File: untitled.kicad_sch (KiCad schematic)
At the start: 39 parts, among them U17 OPA388, U3 MAX9939, U4 TLV3501AID, U5 DGS0010A, U7 ADC10065

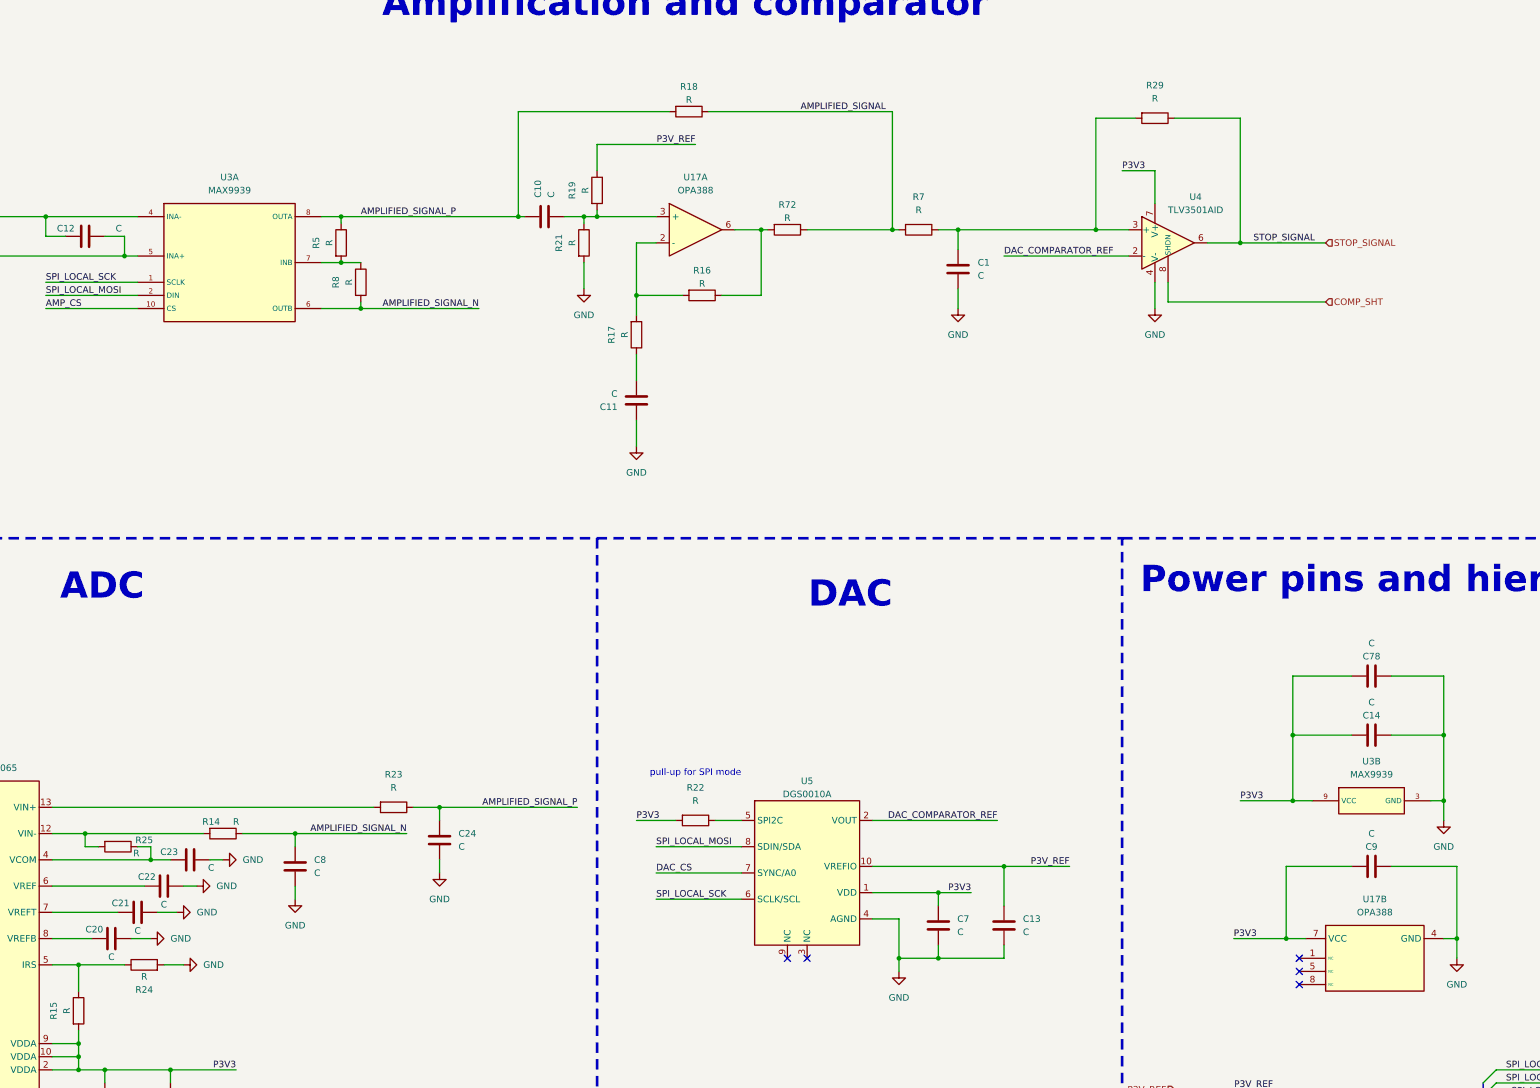
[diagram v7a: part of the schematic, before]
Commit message: most values in schematic filled corrected footprint mistake
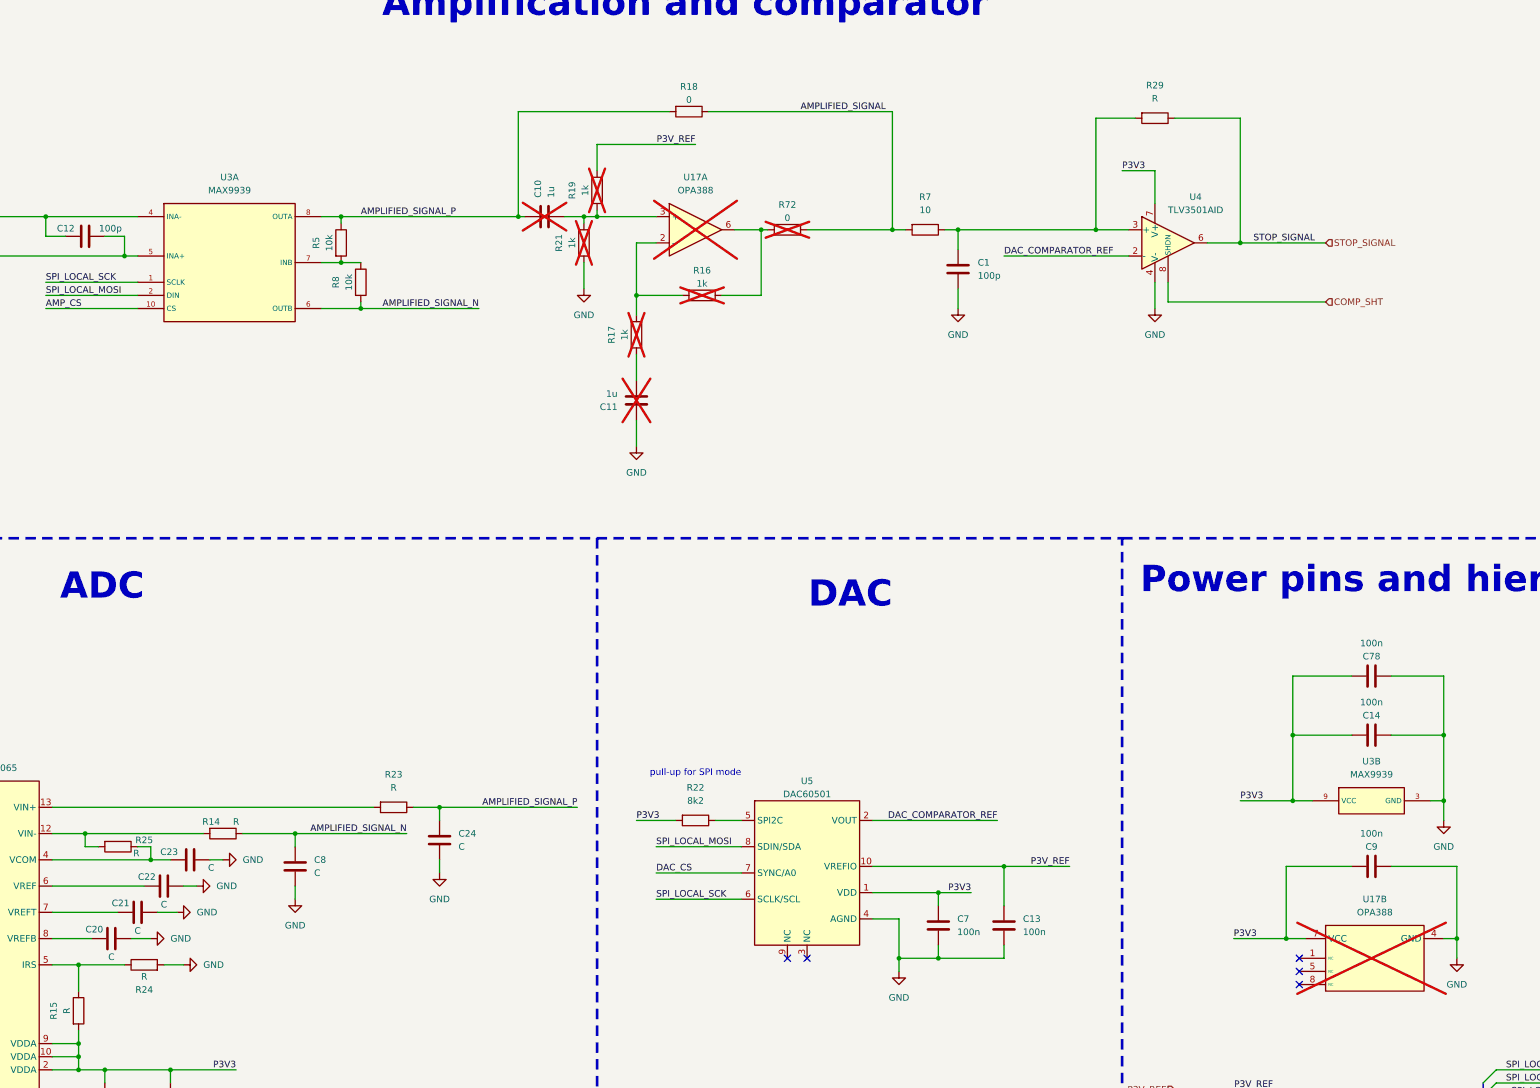
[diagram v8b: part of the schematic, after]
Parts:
- C1, C12: value C -> 100p
- C10, C11: value C -> 1u; now not fitted
- C13, C14, C7, C78, C9: value C -> 100n
- R16, R17, R19, R21: value R -> 1k; now not fitted
- R18: value R -> 0
- R22: value R -> 8k2
- R5, R8: value R -> 10k
- R7: value R -> 10
- R72: value R -> 0; now not fitted
- U17: now not fitted
- U5: value DGS0010A -> DAC60501
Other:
- moved on the sheet: R7
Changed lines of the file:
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@@
 	(wire
 		(pts
-			(xy 255.27 67.31) (xy 256.54 67.31)
+			(xy 255.27 67.31) (xy 257.81 67.31)
 		)
 		(stroke
@@
 	(wire
 		(pts
-			(xy 264.16 67.31) (xy 267.97 67.31)
+			(xy 265.43 67.31) (xy 267.97 67.31)
 		)
 		(stroke
@@
 		(in_bom yes)
 		(on_board yes)
-		(dnp no)
+		(dnp yes)
 		(property "Reference" "R21"
 			(at 190.754 69.85 90)
@@
 			)
 		)
-		(property "Value" "R"
+		(property "Value" "1k"
 			(at 193.294 69.85 90)
 			(effects
@@
 			)
 		)
-		(property "Value" "R"
+		(property "Value" "10k"
 			(at 146.304 69.85 90)
 			(effects
@@
 		(in_bom yes)
 		(on_board yes)
-		(dnp no)
+		(dnp yes)
 		(fields_autoplaced yes)
 		(property "Reference" "U17"
@@
 			)
 		)
-		(property "Datasheet" ""
+		(property "Datasheet" "https://cz.mouser.com/ProductDetail/Texas-Instruments/OPA388IDGKR?qs=sGAEpiMZZMutXGli8Ay4kEuv900fs2zN%2FP2E49NQzzw%3D"
 			(at 212.09 62.23 0)
 			(effects
@@
 		(in_bom yes)
 		(on_board yes)
-		(dnp no)
+		(dnp yes)
 		(fields_autoplaced yes)
 		(property "Reference" "U17"
@@
 			)
 		)
-		(property "Datasheet" ""
+		(property "Datasheet" "https://cz.mouser.com/ProductDetail/Texas-Instruments/OPA388IDGKR?qs=sGAEpiMZZMutXGli8Ay4kEuv900fs2zN%2FP2E49NQzzw%3D"
 			(at 339.09 201.93 0)
 			(effects
@@
 			)
 		)
-		(property "Datasheet" ""
+		(property "Datasheet" "https://cz.mouser.com/ProductDetail/Analog-Devices-Maxim-Integrated/MAX9939AUB%2bT?qs=1eQvB6Dk1vhzbg6od%2Fp2zg%3D%3D"
 			(at 114.3 62.23 0)
 			(effects
@@
 			)
 		)
-		(property "Value" "C"
+		(property "Value" "100n"
 			(at 347.98 184.15 90)
 			(effects
@@
 			)
 		)
-		(property "Value" "C"
+		(property "Value" "100n"
 			(at 347.98 158.75 90)
 			(effects
@@
 			)
 		)
-		(property "Value" "R"
+		(property "Value" "10k"
 			(at 150.114 77.47 90)
 			(effects
@@
 		(in_bom yes)
 		(on_board yes)
-		(dnp no)
+		(dnp yes)
 		(property "Reference" "C10"
 			(at 186.6899 61.1073 0)
@@
 			)
 		)
-		(property "Value" "C"
+		(property "Value" "1u"
 			(at 189.2299 61.1073 0)
 			(effects
@@
 			)
 		)
-		(property "Value" "R"
+		(property "Value" "0"
 			(at 215.9 42.164 90)
 			(effects
@@
 			)
 		)
-		(property "Value" "DGS0010A"
+		(property "Value" "DAC60501"
 			(at 238.76 176.53 0)
 			(effects
@@
 			)
 		)
-		(property "Datasheet" "https://www.ti.com/lit/ds/symlink/dac60501.pdf?ts=1725519797995&ref_url=https%253A%252F%252Fwww.ti.com%252Fproduct%252FDAC60501%253Futm_source%253Dgoogle%2526utm_medium%253Dcpc%2526utm_campaign%253Dasc-null-null-gpn_en-cpc-pf-google-eu%2526utm_content%253Ddac60501%2526ds_k%253DDAC60501%2526dcm%253Dyes%2526gad_source%253D1%2526gclid%253DEAIaIQobChMI3LiUjZ6riAMVb5KDBx30oiEWEAAYASAAEgLsTPD_BwE%2526gclsrc%253Daw.ds"
+		(property "Datasheet" "https://cz.mouser.com/ProductDetail/Texas-Instruments/DAC60501ZDGSR?qs=%252B6g0mu59x7JUdF3YSyQB0g%3D%3D"
 			(at 228.6 177.8 0)
 			(effects
@@
 			)
 		)
-		(property "Value" "C"
+		(property "Value" "100n"
 			(at 280.5227 203.1999 0)
 			(effects
@@
 		(in_bom yes)
 		(on_board yes)
-		(dnp no)
+		(dnp yes)
 		(property "Reference" "R16"
 			(at 218.44 75.184 90)
@@
 			)
 		)
-		(property "Value" "R"
+		(property "Value" "1k"
 			(at 218.44 77.724 90)
 			(effects
@@
 		(in_bom yes)
 		(on_board yes)
-		(dnp no)
+		(dnp yes)
 		(property "Reference" "R17"
 			(at 200.914 87.63 90)
@@
 			)
 		)
-		(property "Value" "R"
+		(property "Value" "1k"
 			(at 203.454 87.63 90)
 			(effects
@@
 			)
 		)
-		(property "Value" "C"
+		(property "Value" "100p"
 			(at 106.172 67.056 90)
 			(effects
@@
 			)
 		)
-		(property "Datasheet" ""
+		(property "Datasheet" "https://cz.mouser.com/ProductDetail/Analog-Devices-Maxim-Integrated/MAX9939AUB%2bT?qs=1eQvB6Dk1vhzbg6od%2Fp2zg%3D%3D"
 			(at 341.63 175.26 0)
 			(effects
@@
 			)
 		)
-		(property "Value" "C"
+		(property "Value" "100n"
 			(at 267.8227 203.1999 0)
 			(effects
@@
 			)
 		)
-		(property "Value" "R"
+		(property "Value" "8k2"
 			(at 217.17 177.8 90)
 			(effects
@@
 	(symbol
 		(lib_id "Device:R")
-		(at 260.35 67.31 270)
+		(at 261.62 67.31 270)
 		(unit 1)
 		(exclude_from_sim no)
@@
 		(fields_autoplaced yes)
 		(property "Reference" "R7"
-			(at 260.35 60.96 90)
+			(at 261.62 60.96 90)
 			(effects
 				(font
@@
 			)
 		)
-		(property "Value" "R"
-			(at 260.35 63.5 90)
+		(property "Value" "10"
+			(at 261.62 63.5 90)
 			(effects
 				(font
@@
 		)
 		(property "Footprint" "Resistor_SMD:R_0603_1608Metric_Pad0.98x0.95mm_HandSolder"
-			(at 260.35 65.532 90)
+			(at 261.62 65.532 90)
 			(effects
 				(font
@@
 		)
 		(property "Datasheet" "~"
-			(at 260.35 67.31 0)
+			(at 261.62 67.31 0)
 			(effects
 				(font
@@
 		)
 		(property "Description" "Resistor"
-			(at 260.35 67.31 0)
+			(at 261.62 67.31 0)
 			(effects
 				(font
@@
 		(in_bom yes)
 		(on_board yes)
-		(dnp no)
+		(dnp yes)
 		(property "Reference" "R19"
 			(at 193.294 59.69 90)
@@
 			)
 		)
-		(property "Value" "R"
+		(property "Value" "1k"
 			(at 195.834 59.69 90)
 			(effects
@@
 			)
 		)
-		(property "Value" "C"
+		(property "Value" "100n"
 			(at 347.98 147.32 90)
 			(effects
@@
 		(in_bom yes)
 		(on_board yes)
-		(dnp no)
+		(dnp yes)
 		(property "Reference" "C11"
 			(at 202.0773 101.6001 0)
@@
 			)
 		)
-		(property "Value" "C"
+		(property "Value" "1u"
 			(at 202.0773 99.0601 0)
 			(effects
@@
 			)
 		)
-		(property "Value" "C"
+		(property "Value" "100p"
 			(at 271.78 76.1999 0)
 			(effects
@@
 		(in_bom yes)
 		(on_board yes)
-		(dnp no)
+		(dnp yes)
 		(property "Reference" "R72"
 			(at 234.95 62.484 90)
@@
 			)
 		)
-		(property "Value" "R"
+		(property "Value" "0"
 			(at 234.95 65.024 90)
 			(effects
